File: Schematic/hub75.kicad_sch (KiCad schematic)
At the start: 35 parts, among them J1 HUB75_DATA, J20 WS2812B_DATA, J21 WS2812B_PWR, J3 HUB75_PWR, U1 74LS08

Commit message: Added level shifter (may or may not use) other minor fixes
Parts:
- removed J20: WS2812B_DATA, Connector_JST:JST_VH_B2P-VH-B_1x02_P3.96mm_Vertical, symbol Connector_Generic:Conn_01x02
- removed J21: WS2812B_PWR, Connector_JST:JST_VH_B2P-VH-B_1x02_P3.96mm_Vertical, symbol Connector_Generic:Conn_01x02
- removed R67: 7.5k, LED_SMD:LED_1206_3216Metric_Pad1.42x1.75mm_HandSolder, symbol Device:R
- removed R68: 3k, LED_SMD:LED_1206_3216Metric_Pad1.42x1.75mm_HandSolder, symbol Device:R

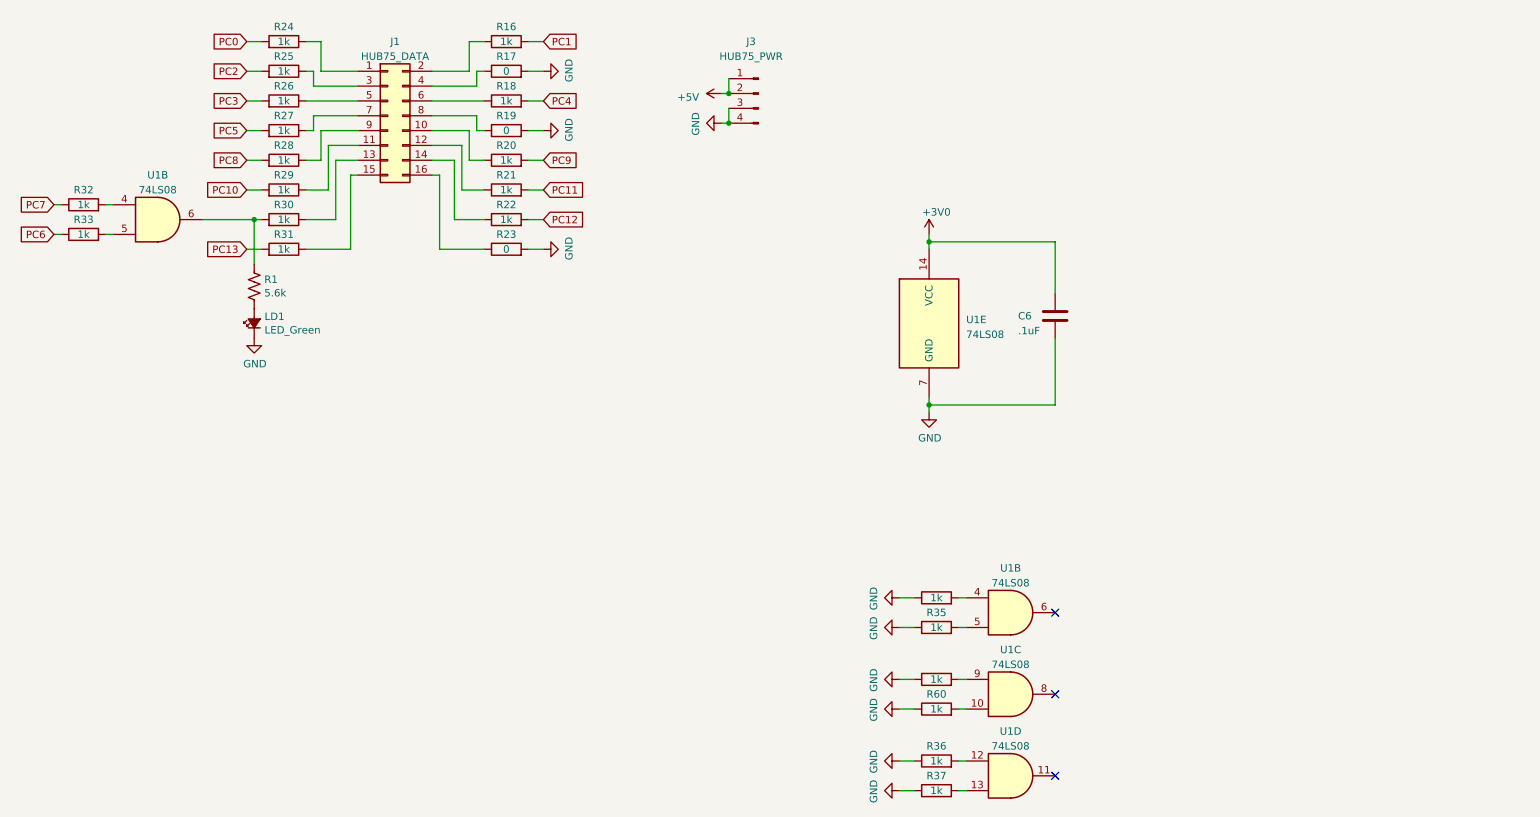
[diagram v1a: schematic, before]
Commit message: relabeld all of the components so they have more resonable numbers
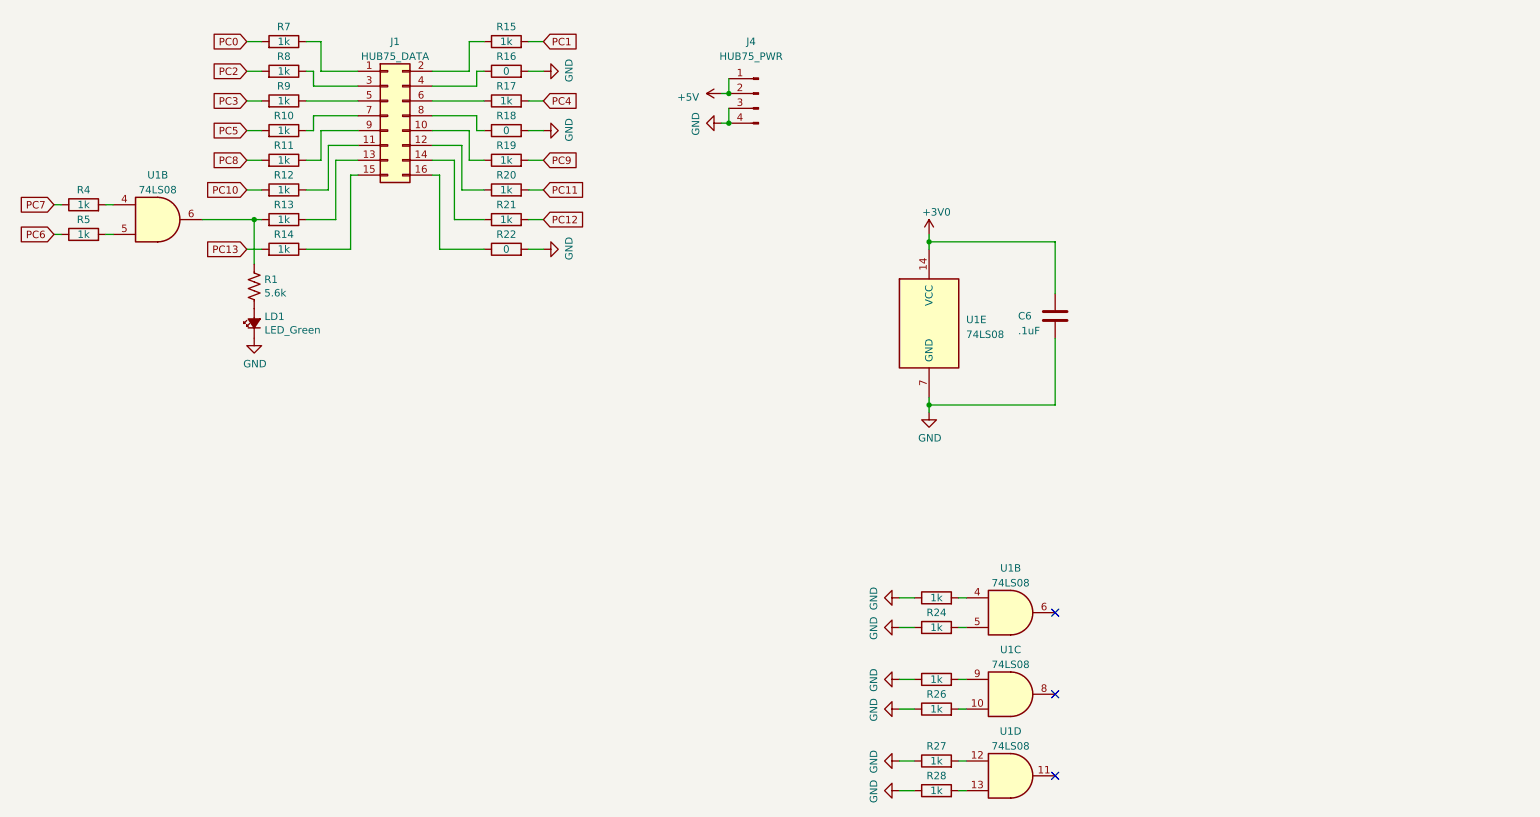
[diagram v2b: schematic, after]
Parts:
- renumbered J3 to J4, R27 to R10, R28 to R11, R29 to R12, R30 to R13, R31 to R14, R16 to R15, R17 to R16, R18 to R17, R19 to R18, R20 to R19, R21 to R20, R22 to R21, R23 to R22, R34 to R23, R35 to R24, R59 to R25, R60 to R26, R36 to R27, R37 to R28, R32 to R4, R33 to R5, R24 to R7, R25 to R8, R26 to R9
